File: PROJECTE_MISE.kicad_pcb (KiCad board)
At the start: 2 copper layers, 75 x 80 mm, 37 parts, among them IC1 MSP430FR2355TPT, J1 conn_DFrobot, J2 ESP01_WiFi_mod, J3 Conn_TX_TP, J4 conn_ACLK_{TP}, J5 conn_SMCLK_{TP}, J6 Conn_RX_TP, J7 conn_SBW, SW1 ~{RST_{MSP}}, U1 LMV324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

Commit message: modificacions layout
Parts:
- Y2: footprint KiCad:LFXTAL002997Bulk -> KiCad:LFXTAL002997Bulk_modificat
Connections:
- RV1 pad 1: unconnected-(RV1-Pad1) -> /LDR_{L}
- RV2 pad 1: unconnected-(RV2-Pad1) -> /LDR_{R}
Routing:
- net /I2C_SCL: track 109.9 -> 93.6 mm
- net /I2C_SDA: track 96.2 -> 83.2 mm, vias 4 -> 3
- net /LDR_{R}: track 43.0 -> 49.0 mm
- net /LDR_{L}: track 42.9 -> 48.9 mm
- net /JTK_{SEL}: track 45.9 -> 47.2 mm

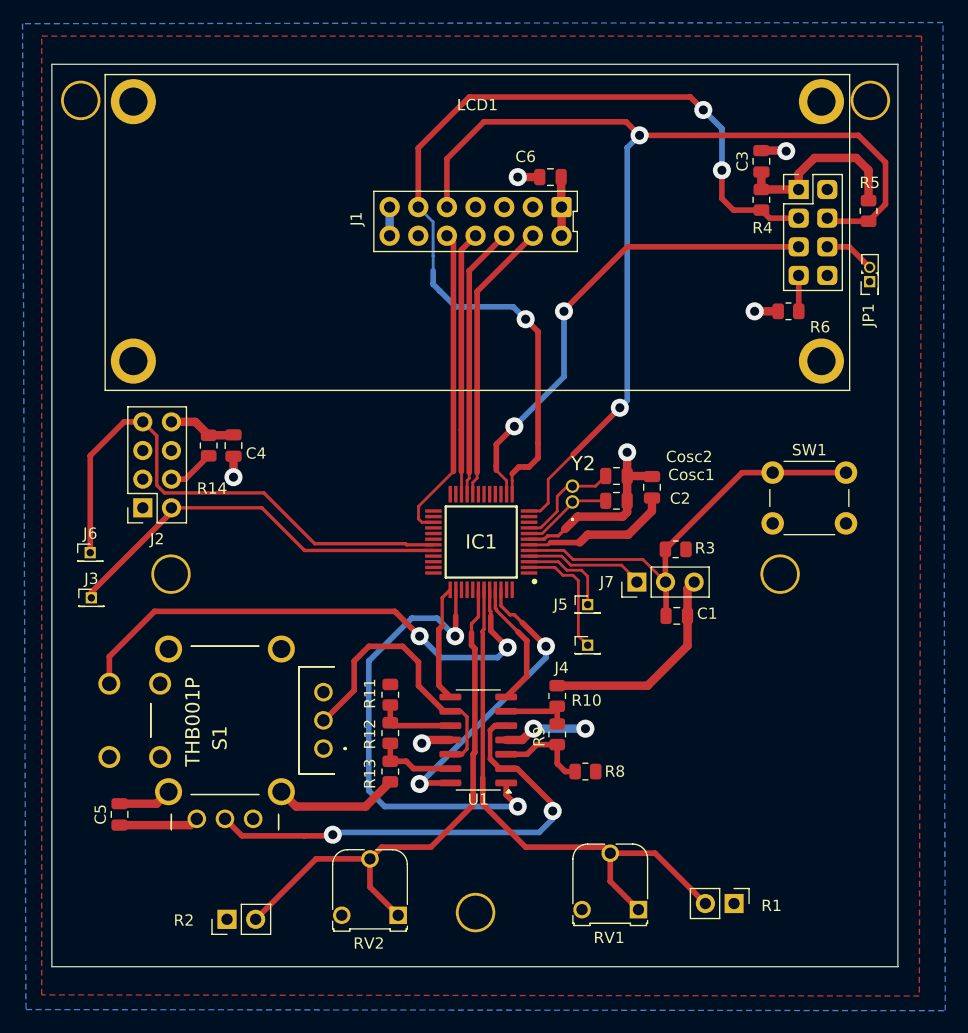
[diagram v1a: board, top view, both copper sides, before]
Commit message: layout 0 errors 0 warnings
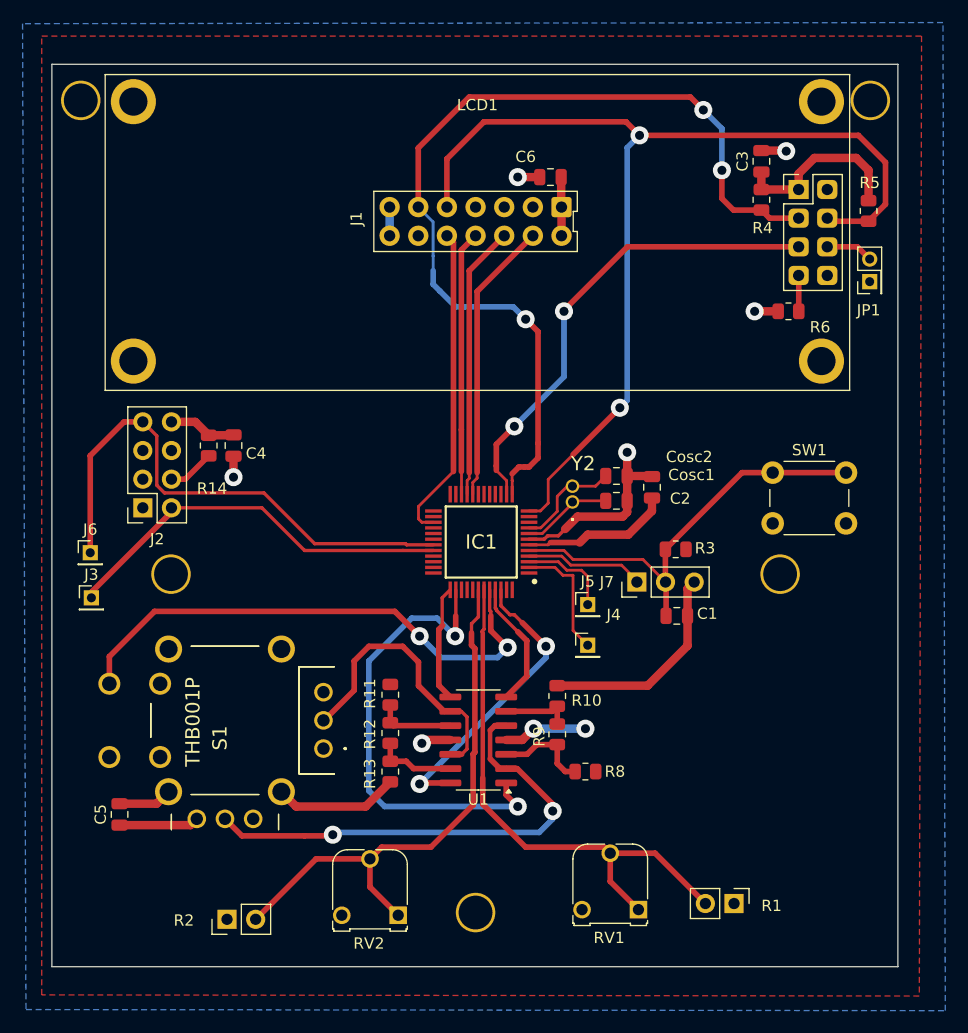
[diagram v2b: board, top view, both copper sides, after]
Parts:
- J3, J4, J5, J6: footprint Connector_PinHeader_1.27mm:PinHeader_1x01_P1.27mm_Vertical -> Connector_PinHeader_2.00mm:PinHeader_1x01_P2.00mm_Vertical
- JP1: footprint Connector_PinHeader_1.27mm:PinHeader_2x01_P1.27mm_Vertical -> Connector_PinHeader_2.00mm:PinHeader_2x01_P2.00mm_Vertical

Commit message: layout finished 0 errors, 0 warnings and solved problems
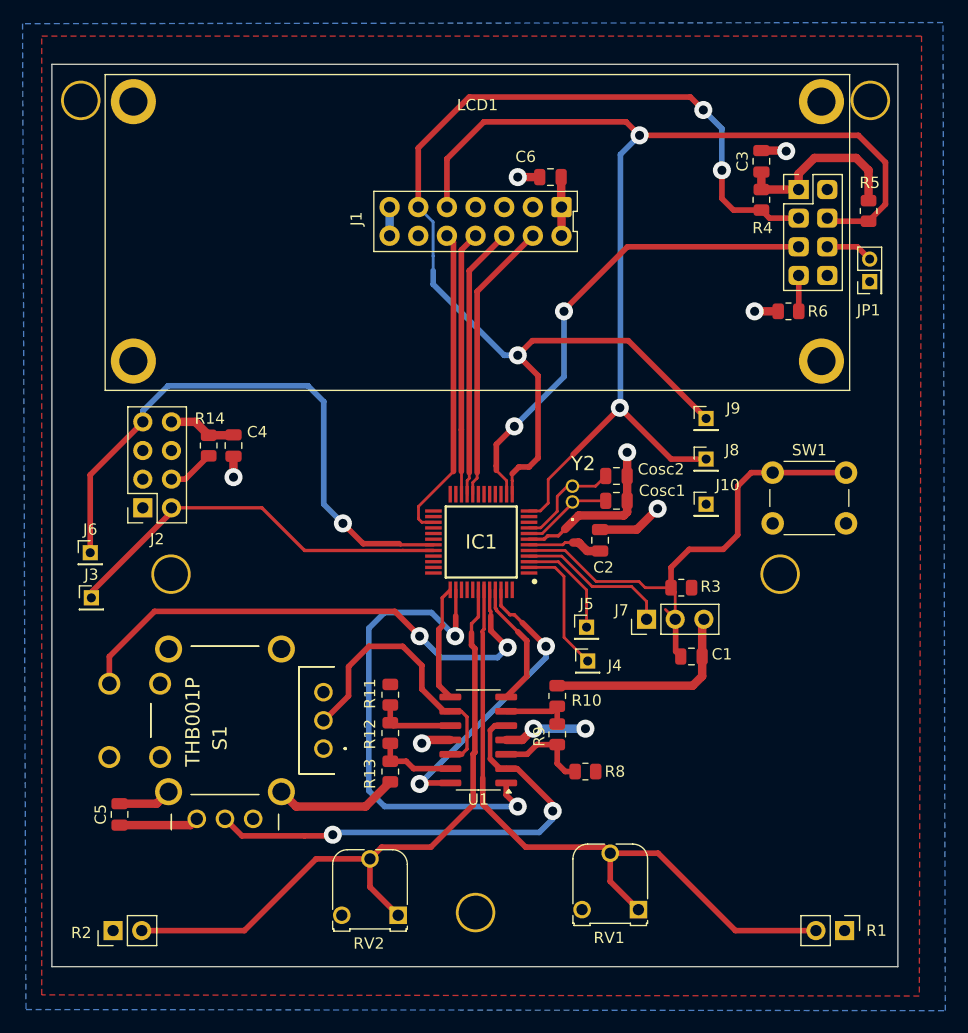
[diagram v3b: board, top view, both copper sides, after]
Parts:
- added J10: Conn_01x01_Pin, Connector_PinHeader_2.00mm:PinHeader_1x01_P2.00mm_Vertical, F.Cu at (127.0, 98.5)
- added J8: SCL_TP, Connector_PinHeader_2.00mm:PinHeader_1x01_P2.00mm_Vertical, F.Cu at (127.0, 94.5)
- added J9: SDA_TP, Connector_PinHeader_2.00mm:PinHeader_1x01_P2.00mm_Vertical, F.Cu at (127.0, 90.9)
- moved R2 10.1 mm to (74.4, 136.3)
- moved R1 10.1 mm to (139.3, 136.3)
- moved C2 6.58 mm to (117.6, 101.7)
- moved C1 3.83 mm to (125.7, 112.0)
- moved R3 3.44 mm to (124.8, 105.9)
- moved J7 3.41 mm to (121.7, 108.7)
- moved J5 2.00 mm to (116.4, 109.4)
- moved J4 1.40 mm to (116.5, 112.4)
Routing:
- net /I2C_SDA: track 83.2 -> 101.0 mm
- net /LDR_{L}: track 48.9 -> 59.7 mm
- net /LDR_{R}: track 49.0 -> 59.5 mm
- net /I2C_SCL: track 93.6 -> 103.1 mm
- net /SBW_{TDIO}: track 38.0 -> 45.0 mm
- net +3V3: track 55.2 -> 48.6 mm
- net /RX_{ESP}: track 47.3 -> 52.4 mm, vias 0 -> 1
- net GND: track 65.3 -> 68.4 mm, vias 6 -> 7
- net /SBW_{TCK}: track 11.1 -> 13.7 mm
- net /JTK_{F}: track 41.8 -> 43.9 mm
- net /SMCLK_{TP}: track 8.24 -> 9.44 mm
- net /ACLK_{TP}: track 10.9 -> 11.8 mm

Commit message: final layout + gerbers
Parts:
- added C7: 100n, Capacitor_SMD:C_0805_2012Metric, F.Cu at (112.3, 119.4)
- added G***: LOGO, LOGO, F.Cu at (132.0, 118.0)
- added REF**: WEEE-Logo_4.2x6mm_SilkScreen, Symbol:WEEE-Logo_4.2x6mm_SilkScreen, F.Cu at (87.5, 65.0)
- added REF**: CE-Logo_8.5x6mm_SilkScreen, Symbol:CE-Logo_8.5x6mm_SilkScreen, F.Cu at (79.1, 69.6)
- added REF**: RoHS-Logo_6mm_SilkScreen, Symbol:RoHS-Logo_6mm_SilkScreen, F.Cu at (85.4, 78.6)
- added REF**: FCC-Logo_7.3x6mm_SilkScreen, Symbol:FCC-Logo_7.3x6mm_SilkScreen, F.Cu at (95.1, 65.2)
- R14: value R -> 10K
- moved R9 5.62 mm to (118.2, 115.4), turned to 180 degrees
- moved R8 4.96 mm to (120.0, 118.9)
- moved C1 3.11 mm to (123.4, 109.9)
- moved C5 2.88 mm to (77.4, 127.6)
- moved J7 2.41 mm to (119.9, 107.1)
- moved R3 2.13 mm to (123.4, 104.3)
- moved R10 1.62 mm to (112.3, 116.1), turned to 0 degrees
- moved JP1 0.47 mm to (141.3, 79.2)
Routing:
- net GND: track 68.4 -> 55.4 mm, vias 7 -> 9
- net /TH_{F}: track 8.45 -> 18.6 mm
- net /TH_{B}: track 6.29 -> 9.79 mm
- net /SBW_{TCK}: track 13.7 -> 10.3 mm
- net /SBW_{TDIO}: track 45.0 -> 42.1 mm
- net +3V3: track 48.6 -> 46.2 mm
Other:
- board text added: "David Garcia Perez Aidar Iglesias Bolos MiSE 2024-25 Universitat de Barcelona"

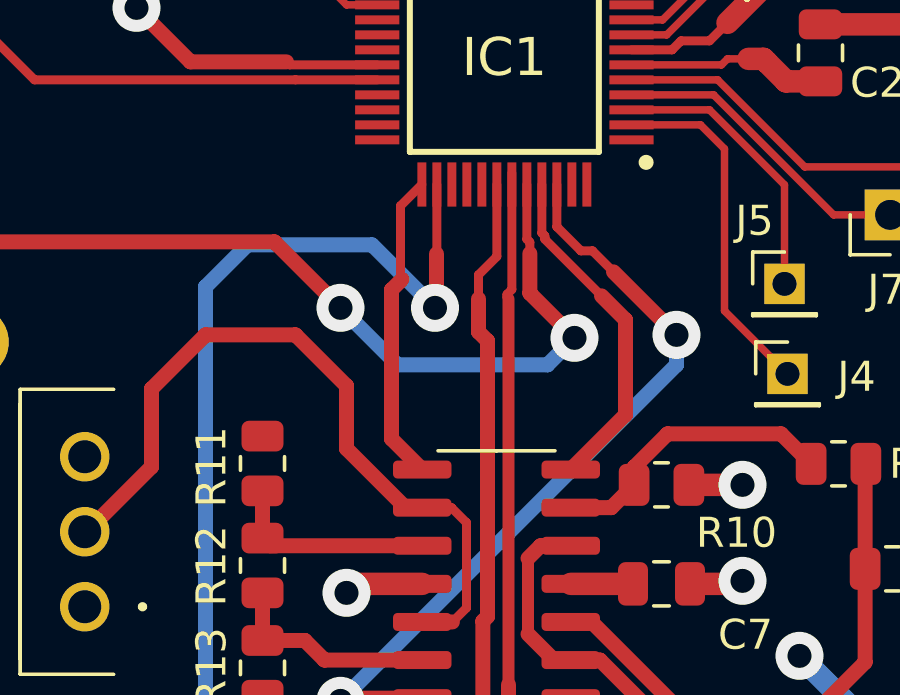
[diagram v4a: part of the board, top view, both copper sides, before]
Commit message: fixes layout + pending VCC LED, C ESP & redraw gerbers
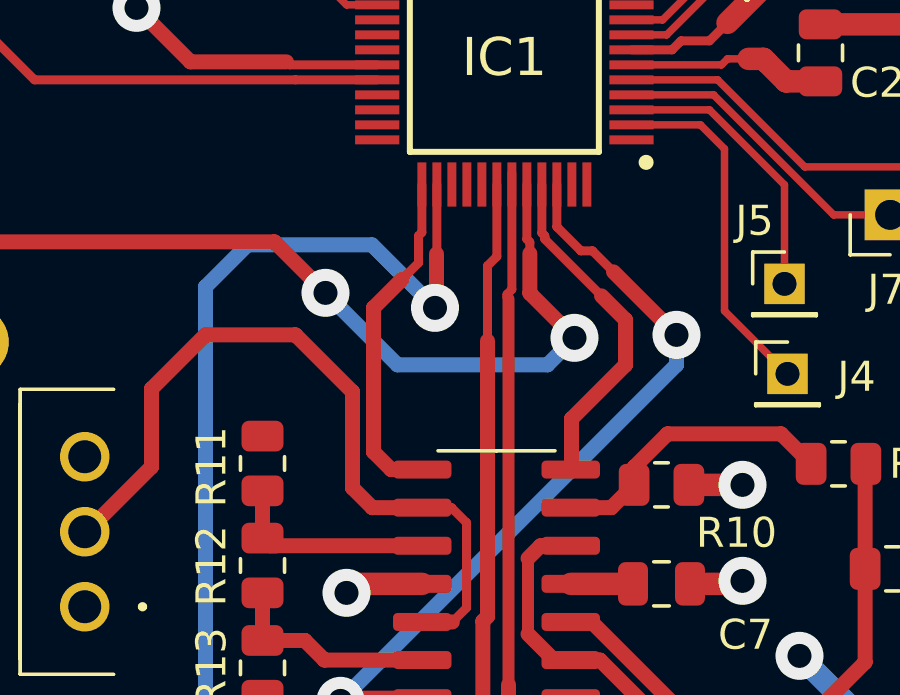
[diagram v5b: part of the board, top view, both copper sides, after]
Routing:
- net /JTK_{R}: track 10.4 -> 11.4 mm
- net /AO1: track 25.3 -> 25.9 mm

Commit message: layout finished
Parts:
- removed REF**: WEEE-Logo_4.2x6mm_SilkScreen, Symbol:WEEE-Logo_4.2x6mm_SilkScreen
- removed REF**: CE-Logo_8.5x6mm_SilkScreen, Symbol:CE-Logo_8.5x6mm_SilkScreen
- removed REF**: RoHS-Logo_6mm_SilkScreen, Symbol:RoHS-Logo_6mm_SilkScreen
- removed REF**: FCC-Logo_7.3x6mm_SilkScreen, Symbol:FCC-Logo_7.3x6mm_SilkScreen
- added C8: 100n, Capacitor_SMD:C_0805_2012Metric, F.Cu at (113.2, 77.5)
- added D1: LED, LED_SMD:LED_0805_2012Metric, F.Cu at (71.6, 71.3)
- added R7: 100, Resistor_SMD:R_0805_2012Metric, F.Cu at (71.6, 75.5)
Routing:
- net +3V3: track 46.2 -> 97.9 mm, vias 2 -> 3
- net GND: track 55.4 -> 59.5 mm, vias 9 -> 11
- net /LED_PS: track 0.00 -> 2.35 mm

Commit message: update R value LED_PS + update gerber files
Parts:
- R7: value 100 -> 110R

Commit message: gerbers update and final version
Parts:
- moved J2 1.14 mm to (76.4, 99.7)
- moved C4 1.04 mm to (84.1, 93.0)
- moved R14 0.85 mm to (82.1, 93.0)
- moved J3 0.61 mm to (71.9, 106.7)
- moved J6 0.60 mm to (71.8, 102.8)
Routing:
- net /~{EN_{ESP}}: track 4.16 -> 5.31 mm
- net /RX_{ESP}: track 52.4 -> 53.3 mm
- net +3V3: track 97.9 -> 97.1 mm
- net /TX_{ESP}: track 35.7 -> 35.0 mm
